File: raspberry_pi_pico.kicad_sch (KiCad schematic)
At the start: 72 parts, among them J10 Conn_01x20_Socket, J2 Conn_02x20_Counter_Clockwise, J3 Conn_02x20_Counter_Clockwise, J4 Conn_01x20_Socket, J7 Conn_01x01_Pin, U3 Pico

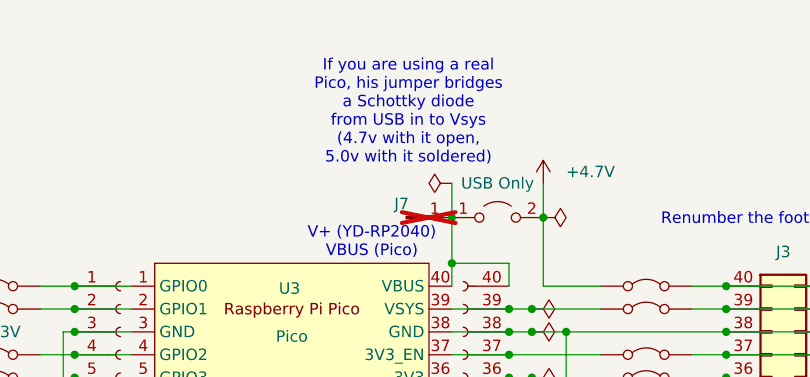
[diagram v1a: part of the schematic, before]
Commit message: Added some power traces
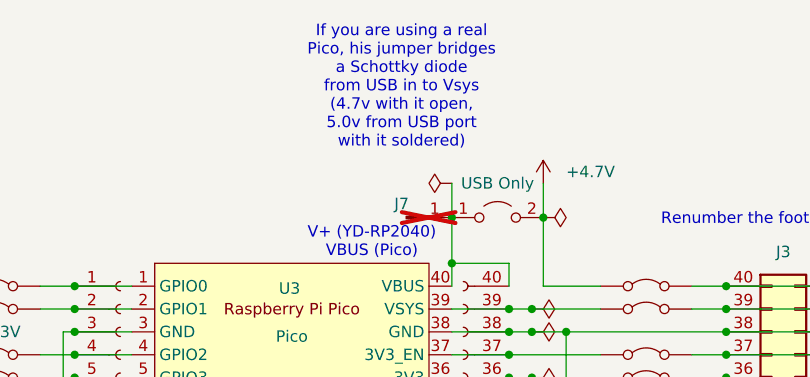
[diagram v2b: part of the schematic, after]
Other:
- note added: "If you are using a real Pico, his jumper bridges a Schottky diode from USB in to Vsys (4.7v with it open, 5.0v from USB port with it soldered)"
- note removed: "If you are using a real Pico, his jumper bridges a Schottky diode from USB in to Vsys (4.7v with it open, 5.0v with it soldered)"
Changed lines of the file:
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@@
 		)
 	)
-	(text "If you are using a real\nPico, his jumper bridges\na Schottky diode\nfrom USB in to Vsys\n(4.7v with it open,\n5.0v with it soldered)"
+	(text "If you are using a real\nPico, his jumper bridges\na Schottky diode\nfrom USB in to Vsys\n(4.7v with it open,\n5.0v from USB port\nwith it soldered)"
 		(exclude_from_sim no)
-		(at 151.384 48.006 0)
+		(at 150.622 45.212 0)
 		(effects
 			(font
@@
 			(justify left bottom)
 		)
-		(property "Netclass" "5V"
+		(property "Netclass" "5V0"
 			(at 201.3585 64.77 0)
 			(effects
@@
 			)
 		)
+	)
+	(netclass_flag ""
+		(length 2.54)
+		(shape round)
+		(at 158.75 64.77 0)
+		(fields_autoplaced yes)
+		(effects
+			(font
+				(size 1.27 1.27)
+			)
+			(justify left bottom)
+		)
+		(property "Netclass" "5V0"
+			(at 159.4485 62.23 0)
+			(effects
+				(font
+					(size 1.27 1.27)
+				)
+				(justify left)
+				(hide yes)
+			)
+		)
+		(property "Component Class" ""
+			(at -91.44 -1.27 0)
+			(effects
+				(font
+					(size 1.27 1.27)
+					(italic yes)
+				)
+			)
+		)

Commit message: 328 warnings
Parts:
- J10, J2, J3, J4: now not fitted
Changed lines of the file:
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@@
 		(in_bom yes)
 		(on_board yes)
-		(dnp no)
+		(dnp yes)
 		(property "Reference" "J4"
 			(at 120.65 90.1699 0)
@@
 		(in_bom yes)
 		(on_board yes)
-		(dnp no)
+		(dnp yes)
 		(fields_autoplaced yes)
 		(property "Reference" "J2"
@@
 		(in_bom yes)
 		(on_board yes)
-		(dnp no)
+		(dnp yes)
 		(fields_autoplaced yes)
 		(property "Reference" "J3"
@@
 		(in_bom yes)
 		(on_board yes)
-		(dnp no)
+		(dnp yes)
 		(property "Reference" "J10"
 			(at 156.21 90.1699 0)
